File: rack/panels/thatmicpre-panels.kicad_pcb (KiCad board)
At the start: 2 copper layers, 87.9 x 78 mm, 2 parts

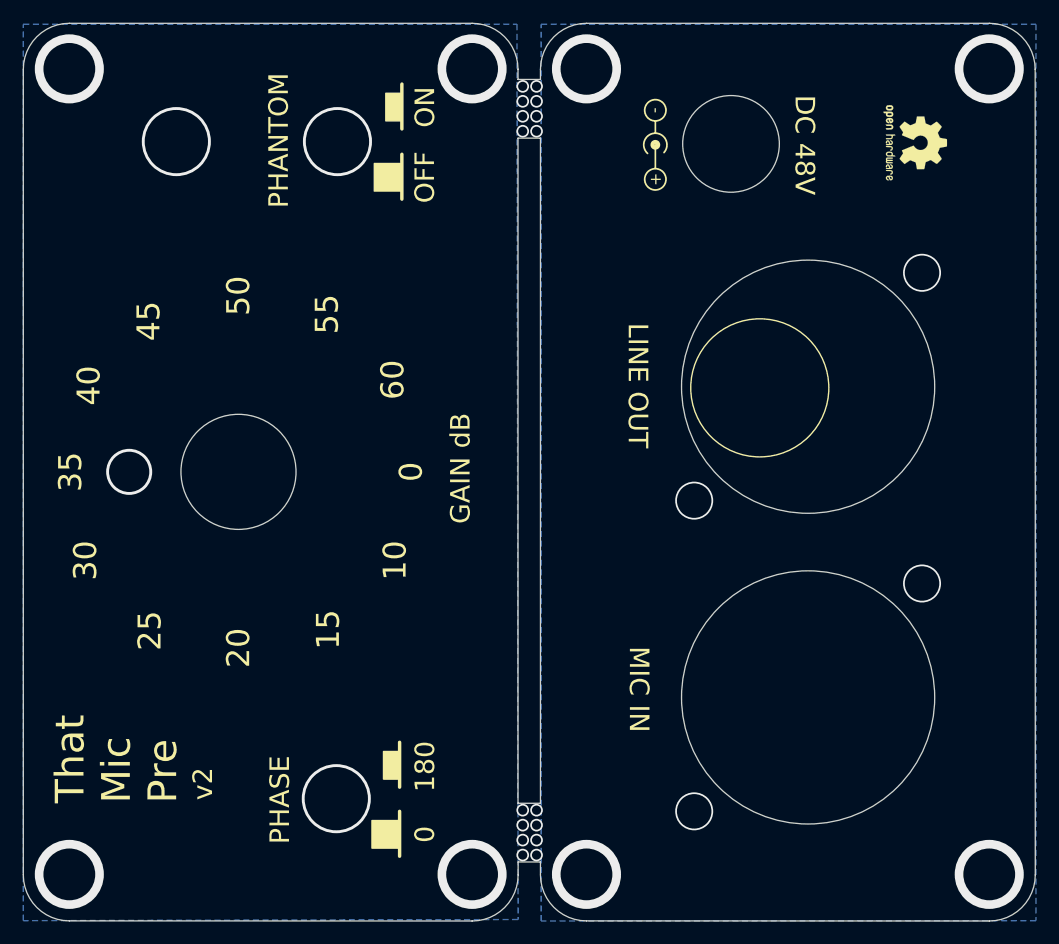
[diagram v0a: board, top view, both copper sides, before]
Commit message: Move the hole of panels up by 1mm. For the new case
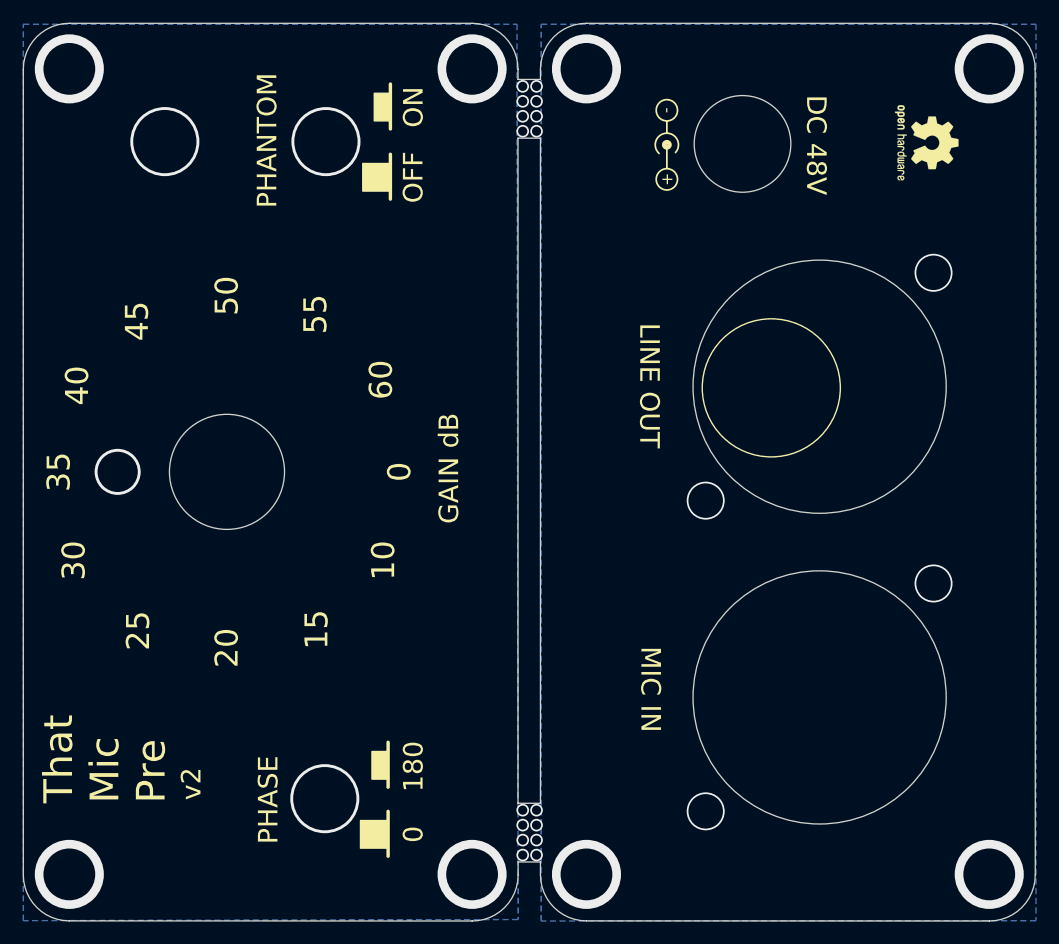
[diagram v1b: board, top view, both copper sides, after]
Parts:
- moved LOGO4 1.00 mm to (158.7, 65.0)
- moved REF** 1.00 mm to (181.2, 64.8)
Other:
- outline, holes or cut-outs redrawn
